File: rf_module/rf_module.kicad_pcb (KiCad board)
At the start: 4 copper layers, 54.5 x 25 mm, 98 parts, among them J1 Conn_01x14, J2 UHF, Q1 SQ2318, U1 LP2985-1.8, U2 TYKTBCSANF-26.000000, U3 NL17SV04XV5T2G, U4 Si4463, U5 TQP3M9036, U6 LFCG-490+, U7 F2972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

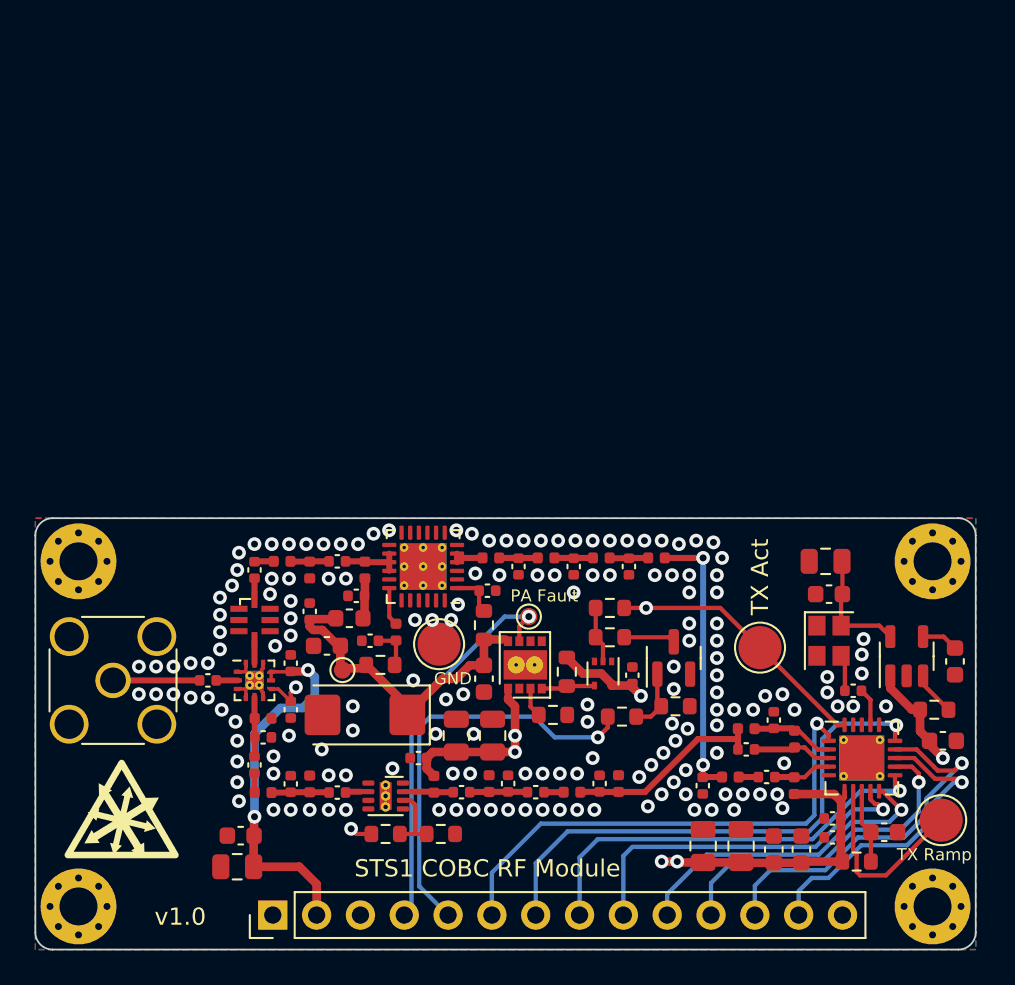
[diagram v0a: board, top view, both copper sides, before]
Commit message: feat: implement LNA activation on RX and PA_Enable in schematic (layout TODO)
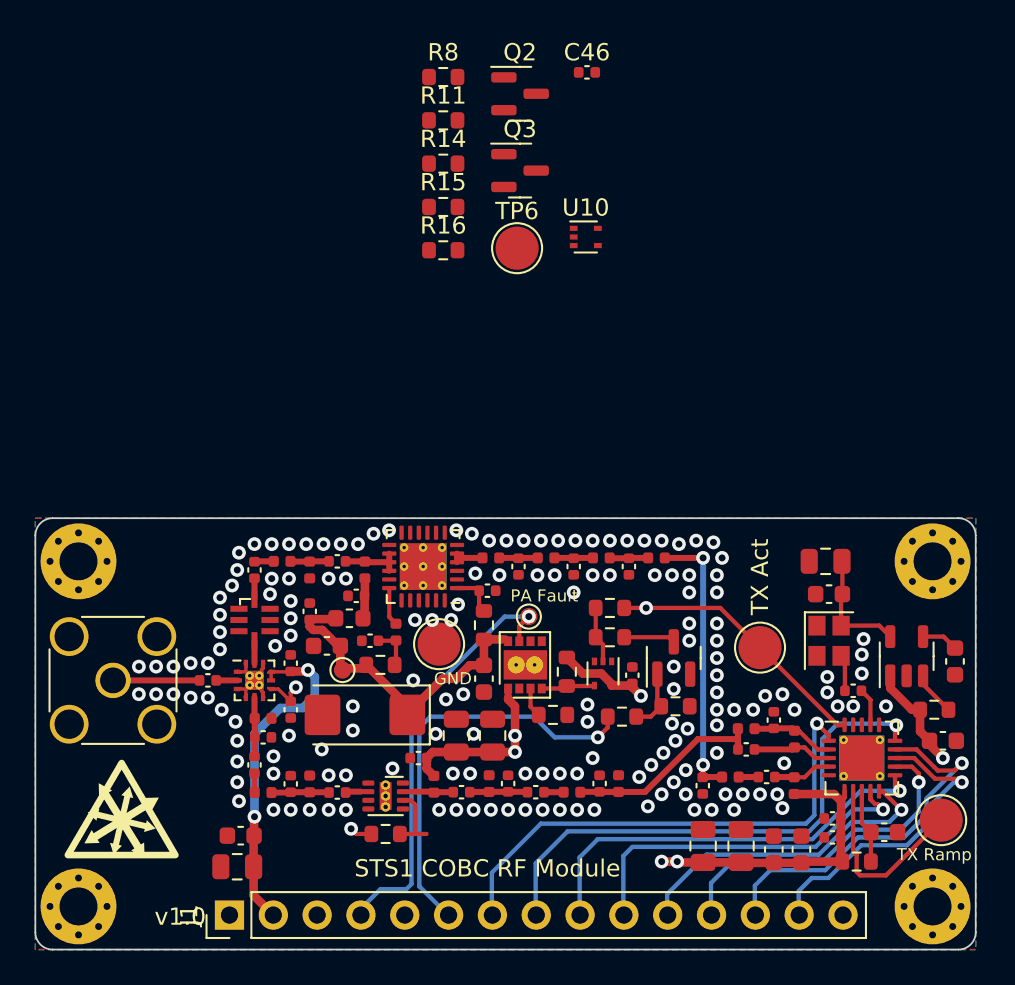
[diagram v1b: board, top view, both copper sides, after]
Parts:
- added C46: 100p, Capacitor_SMD:C_0402_1005Metric, F.Cu at (120.5, 47.2)
- added Q2: SQ2318, Package_TO_SOT_SMD:SOT-23, F.Cu at (116.6, 48.4)
- added Q3: SQ2318, Package_TO_SOT_SMD:SOT-23, F.Cu at (116.6, 52.9)
- added R11: 100, Resistor_SMD:R_0603_1608Metric, F.Cu at (112.1, 49.9)
- added R14: 10k, Resistor_SMD:R_0603_1608Metric, F.Cu at (112.1, 52.5)
- added R15: 10k, Resistor_SMD:R_0603_1608Metric, F.Cu at (112.1, 55.0)
- added R16: 100, Resistor_SMD:R_0603_1608Metric, F.Cu at (112.1, 57.5)
- added TP6: RX_Active, TestPoint:TestPoint_Pad_D2.5mm, F.Cu at (116.4, 57.4)
- added U10: NL17SV04XV5T2G, Package_TO_SOT_SMD:SOT-553, F.Cu at (120.4, 56.7)
- J1: value Conn_01x14 -> Conn_01x15; footprint Connector_PinHeader_2.54mm:PinHeader_1x14_P2.54mm_Vertical -> Connector_PinHeader_2.54mm:PinHeader_1x15_P2.54mm_Vertical
- R8: value 10k -> 100
- moved R8 43.9 mm to (112.1, 47.4)
- moved J1 2.51 mm to (99.8, 96.0)
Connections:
- J1 pad 10: /Si4463_GPIO1 -> /Si4463_GPIO0
- J1 pad 11: /Si4463_SPI_CLK -> /Si4463_GPIO1
- J1 pad 12: /Si4463_SDI -> /Si4463_SPI_CLK
- J1 pad 13: /Si4463_SDO -> /Si4463_SDI
- J1 pad 14: GND -> /Si4463_SDO
- J1 pad 5: /TX_Block -> /PA_Enable
- J1 pad 6: /Si4463_SDN -> /PA_Block
- J1 pad 7: /Si4463_nSEL -> /Si4463_SDN
- J1 pad 8: /Si4463_nIRQ -> /Si4463_nSEL
- J1 pad 9: /Si4463_GPIO0 -> /Si4463_nIRQ
- R2 pad 1: /TX_Block -> /PA_Block
- R7 pad 1: Net-(R7-Pad1) -> Net-(U5-Shut_Down)
- R7 pad 2: /TX_Active -> Net-(R7-Pad2)
- R8 pad 1: Net-(R7-Pad1) -> Net-(Q2-D)
- R8 pad 2: GND -> Net-(R4-Pad2)
- U4 pad 19: unconnected-(U4-Pad19) -> /RX_Active
- U5 pad 6: Net-(R7-Pad1) -> Net-(U5-Shut_Down)
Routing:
- net /TX_Block: track 24.1 -> 0.00 mm, vias 1 -> 0
- net /PA_Block: track 0.00 -> 24.1 mm, vias 0 -> 1
- net Net-(U5-Shut_Down): track 0.00 -> 4.05 mm
- net Net-(R7-Pad1): track 4.05 -> 0.00 mm
- net +5V: track 30.5 -> 33.6 mm
- net /PA_Fault: track 22.8 -> 24.7 mm
- net +3V3: track 104.0 -> 104.8 mm

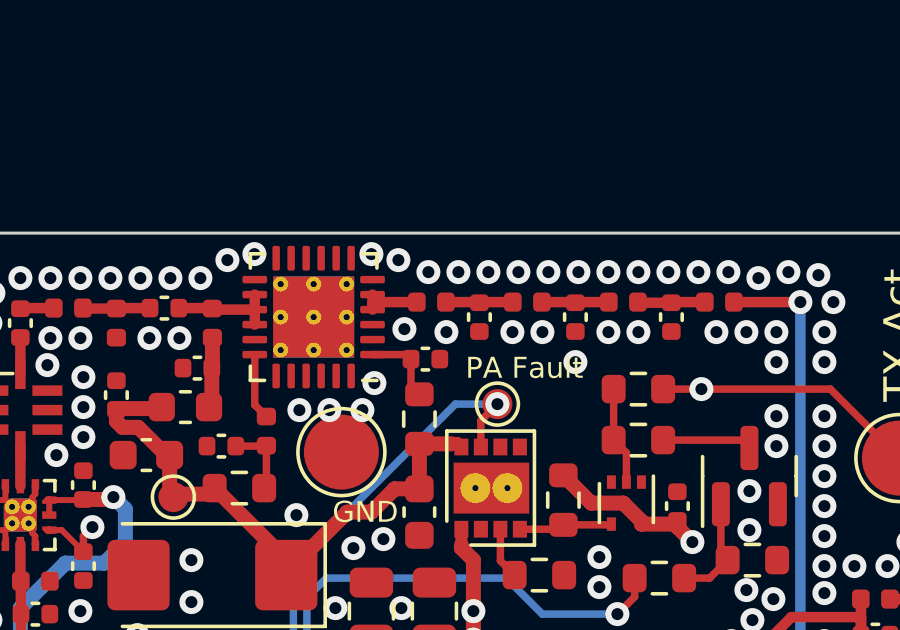
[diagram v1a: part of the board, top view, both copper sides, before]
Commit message: fix: component values of TX PA input matching and filter
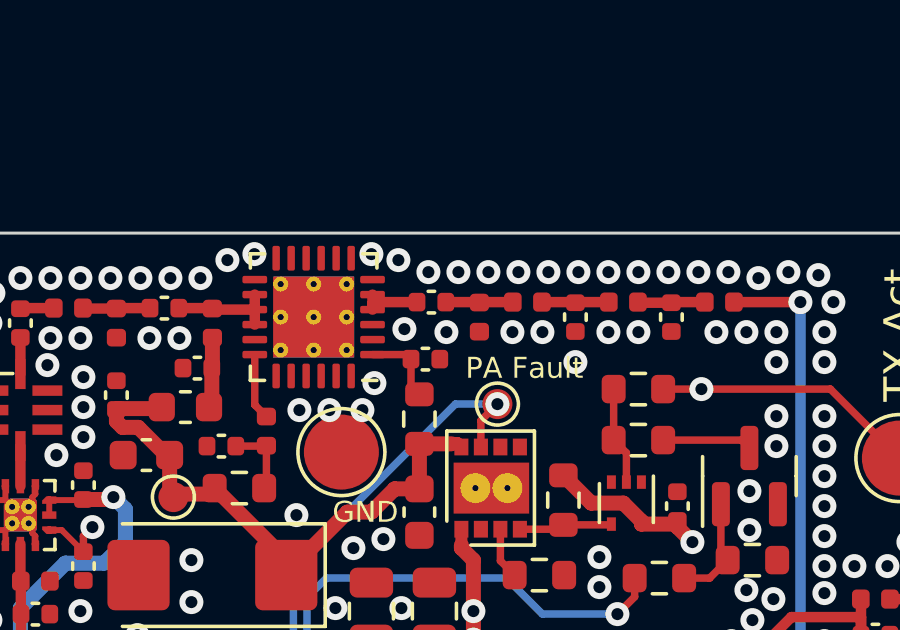
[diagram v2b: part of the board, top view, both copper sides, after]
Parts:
- C2: value 12p -> 7.5p
- C37: value 18p -> 50p
- C4: value 10p -> 7.5p
- L1: value 30n -> 33n
- L16: value 6n -> 4n
- L2: value 36n -> 51n
- L3: value 22n -> 33n
- moved C37 1.68 mm to (114.9, 75.3), turned to 180 degrees
- moved L16 1.68 mm to (116.5, 75.8), turned to 90 degrees
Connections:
- C37 pad 2: GND -> /UHF_PA/RF_Amp_In
- L16 pad 1: /RF_LPF1_Out -> GND
- L16 pad 2: /UHF_PA/RF_Amp_In -> /RF_LPF1_Out
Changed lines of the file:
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@@
         (effects (font (size 1 1) (thickness 0.15)))
     )
-    (fp_text value "36n" (at 0 2.1 90) (layer "F.Fab")
+    (fp_text value "51n" (at 0 2.1 90) (layer "F.Fab")
         (effects (font (size 1 1) (thickness 0.15)))
     )
@@
         (effects (font (size 1 1) (thickness 0.15)))
     )
-    (fp_text value "30n" (at 0 2 90) (layer "F.Fab")
+    (fp_text value "33n" (at 0 2 90) (layer "F.Fab")
         (effects (font (size 1 1) (thickness 0.15)))
     )
@@
         (effects (font (size 1 1) (thickness 0.15)))
     )
-    (fp_text value "12p" (at -2.5 0 90) (layer "F.Fab")
+    (fp_text value "7.5p" (at -2.5 0 90) (layer "F.Fab")
         (effects (font (size 1 1) (thickness 0.15)))
     )
@@
         (effects (font (size 1 1) (thickness 0.15)))
     )
-    (fp_text value "10p" (at -2.6 0 90) (layer "F.Fab")
+    (fp_text value "7.5p" (at -2.6 0 90) (layer "F.Fab")
         (effects (font (size 1 1) (thickness 0.15)))
     )
@@
   )
   (footprint "Capacitor_SMD:C_0402_1005Metric" (layer "F.Cu")
-    (at 116.5 75.8 -90)
+    (at 114.9 75.3 180)
     (descr "Capacitor SMD 0402 (1005 Metric), square (rectangular) end terminal, IPC_7351 nominal, (Body size source: IPC-SM-782 page 76, https://www.pcb-3d.com/wordpress/wp-content/uploads/ipc-sm-782a_amendment_1_and_2.pdf), generated with kicad-footprint-generator")
     (tags "capacitor")
@@
     (property "ki_keywords" "cap capacitor")
     (attr smd)
-    (fp_text reference "C37" (at 0 -1.16 90) (layer "F.SilkS") hide
+    (fp_text reference "C37" (at 0 -1.16) (layer "F.SilkS") hide
         (effects (font (size 1 1) (thickness 0.15)))
     )
-    (fp_text value "18p" (at -2.6 0 90) (layer "F.Fab")
+    (fp_text value "50p" (at -2.6 0) (layer "F.Fab")
         (effects (font (size 1 1) (thickness 0.15)))
     )
-    (fp_text user "${REFERENCE}" (at 0 0 90) (layer "F.Fab")
+    (fp_text user "${REFERENCE}" (at 0 0) (layer "F.Fab")
         (effects (font (size 0.25 0.25) (thickness 0.04)))
     )
@@
     (fp_line (start 0.5 0.25) (end -0.5 0.25)
       (stroke (width 0.1) (type solid)) (layer "F.Fab"))
-    (pad "1" smd roundrect (at -0.48 0 270) (size 0.56 0.62) (layers "F.Cu" "F.Paste" "F.Mask") (roundrect_rratio 0.25)
+    (pad "1" smd roundrect (at -0.48 0 180) (size 0.56 0.62) (layers "F.Cu" "F.Paste" "F.Mask") (roundrect_rratio 0.25)
       (net 57 "/RF_LPF1_Out") (pintype "passive"))
-    (pad "2" smd roundrect (at 0.48 0 270) (size 0.56 0.62) (layers "F.Cu" "F.Paste" "F.Mask") (roundrect_rratio 0.25)
-      (net 2 "GND") (pintype "passive"))
+    (pad "2" smd roundrect (at 0.48 0 180) (size 0.56 0.62) (layers "F.Cu" "F.Paste" "F.Mask") (roundrect_rratio 0.25)
+      (net 62 "/UHF_PA/RF_Amp_In") (pintype "passive"))
     (model "${KICAD6_3DMODEL_DIR}/Capacitor_SMD.3dshapes/C_0402_1005Metric.wrl"
       (offset (xyz 0 0 0))
@@
         (effects (font (size 1 1) (thickness 0.15)))
     )
-    (fp_text value "22n" (at 0 2.1 90) (layer "F.Fab")
+    (fp_text value "33n" (at 0 2.1 90) (layer "F.Fab")
         (effects (font (size 1 1) (thickness 0.15)))
     )
@@
   )
   (footprint "Inductor_SMD:L_0402_1005Metric" (layer "F.Cu")
-    (at 114.9 75.3 180)
+    (at 116.5 75.8 90)
     (descr "Inductor SMD 0402 (1005 Metric), square (rectangular) end terminal, IPC_7351 nominal, (Body size source: http://www.tortai-tech.com/upload/download/2011102023233369053.pdf), generated with kicad-footprint-generator")
     (tags "inductor")
@@
     (property "ki_keywords" "inductor choke coil reactor magnetic")
     (attr smd)
-    (fp_text reference "L16" (at 0 -1.17) (layer "F.SilkS") hide
+    (fp_text reference "L16" (at 0 -1.17 90) (layer "F.SilkS") hide
         (effects (font (size 1 1) (thickness 0.15)))
     )
-    (fp_text value "6n" (at 0 1.7 90) (layer "F.Fab")
+    (fp_text value "4n" (at 0 1.7) (layer "F.Fab")
         (effects (font (size 1 1) (thickness 0.15)))
     )
-    (fp_text user "${REFERENCE}" (at 0 0) (layer "F.Fab")
+    (fp_text user "${REFERENCE}" (at 0 0 90) (layer "F.Fab")
         (effects (font (size 0.25 0.25) (thickness 0.04)))
     )
@@
     (fp_line (start 0.5 0.25) (end -0.5 0.25)
       (stroke (width 0.1) (type solid)) (layer "F.Fab"))
-    (pad "1" smd roundrect (at -0.485 0 180) (size 0.59 0.64) (layers "F.Cu" "F.Paste" "F.Mask") (roundrect_rratio 0.25)
+    (pad "1" smd roundrect (at -0.485 0 90) (size 0.59 0.64) (layers "F.Cu" "F.Paste" "F.Mask") (roundrect_rratio 0.25)
+      (net 2 "GND") (pintype "passive"))
+    (pad "2" smd roundrect (at 0.485 0 90) (size 0.59 0.64) (layers "F.Cu" "F.Paste" "F.Mask") (roundrect_rratio 0.25)
       (net 57 "/RF_LPF1_Out") (pintype "passive"))
-    (pad "2" smd roundrect (at 0.485 0 180) (size 0.59 0.64) (layers "F.Cu" "F.Paste" "F.Mask") (roundrect_rratio 0.25)
-      (net 62 "/UHF_PA/RF_Amp_In") (pintype "passive"))
     (model "${KICAD6_3DMODEL_DIR}/Inductor_SMD.3dshapes/L_0402_1005Metric.wrl"
       (offset (xyz 0 0 0))
